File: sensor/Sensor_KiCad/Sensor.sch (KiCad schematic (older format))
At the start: 32 parts, among them J1 Conn_01x02_Female, J2 Conn_01x02_Female, J3 Conn_01x02_Female, J4 Conn_01x02_Female, J5 Conn_01x02_Female, J6 Conn_01x02_Female, J7 Conn_01x02_Female, J8 Conn_01x02_Female, U1 LM358, U2 LM358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

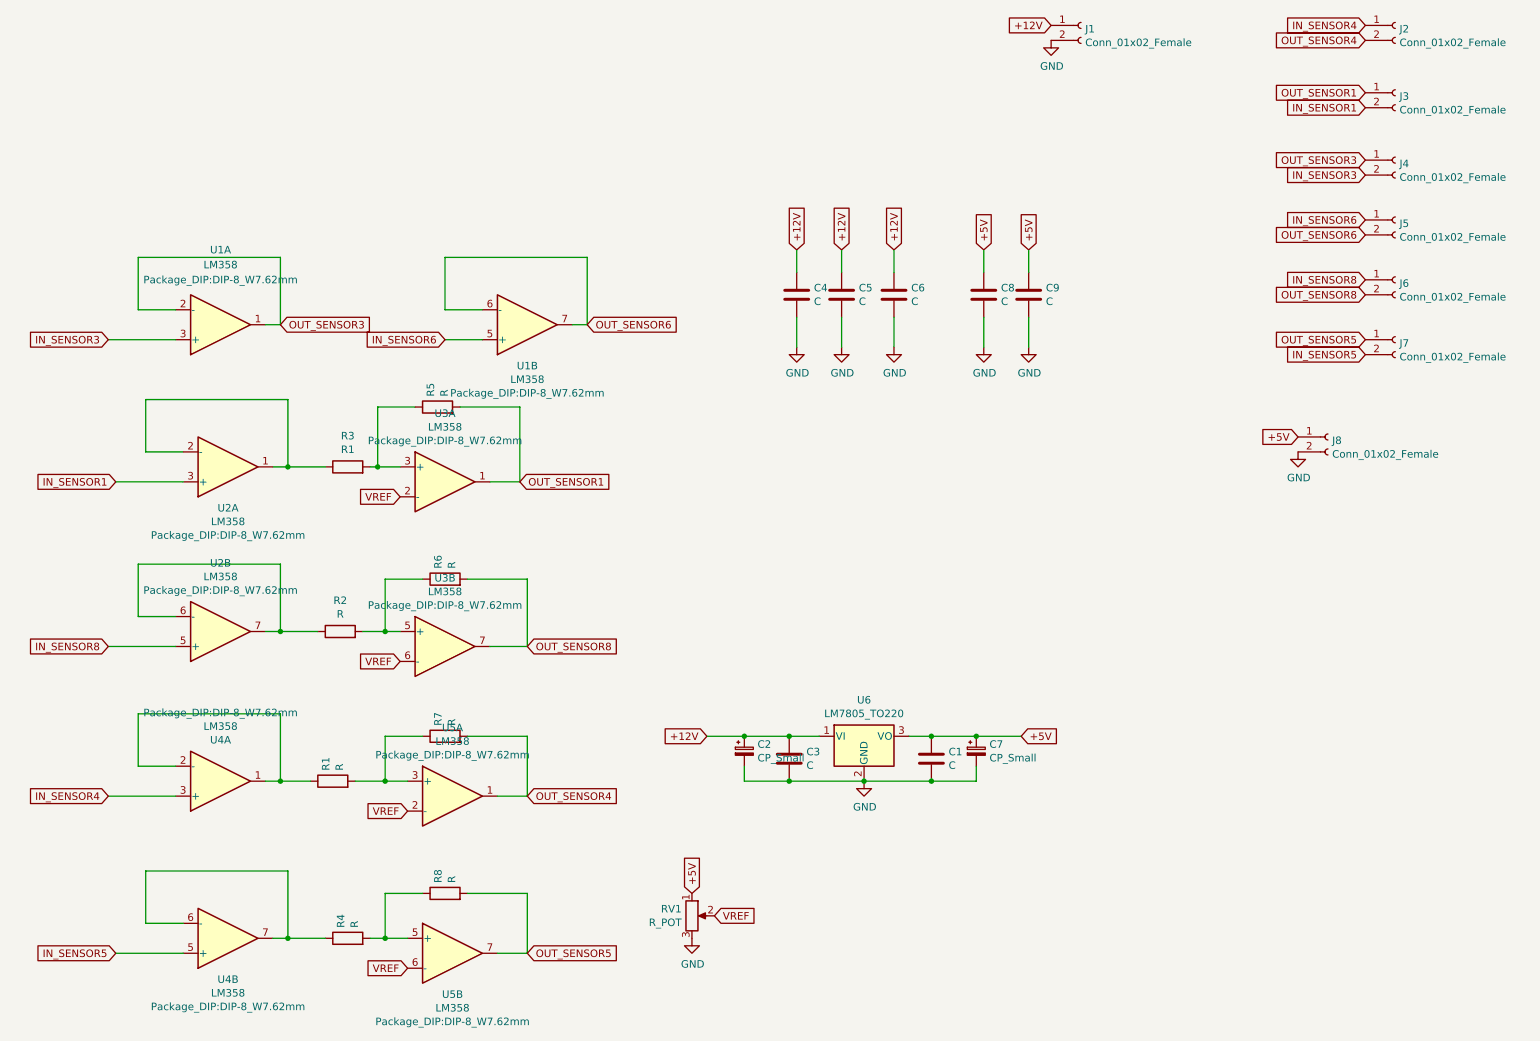
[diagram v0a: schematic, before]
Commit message: Kicad projects finished
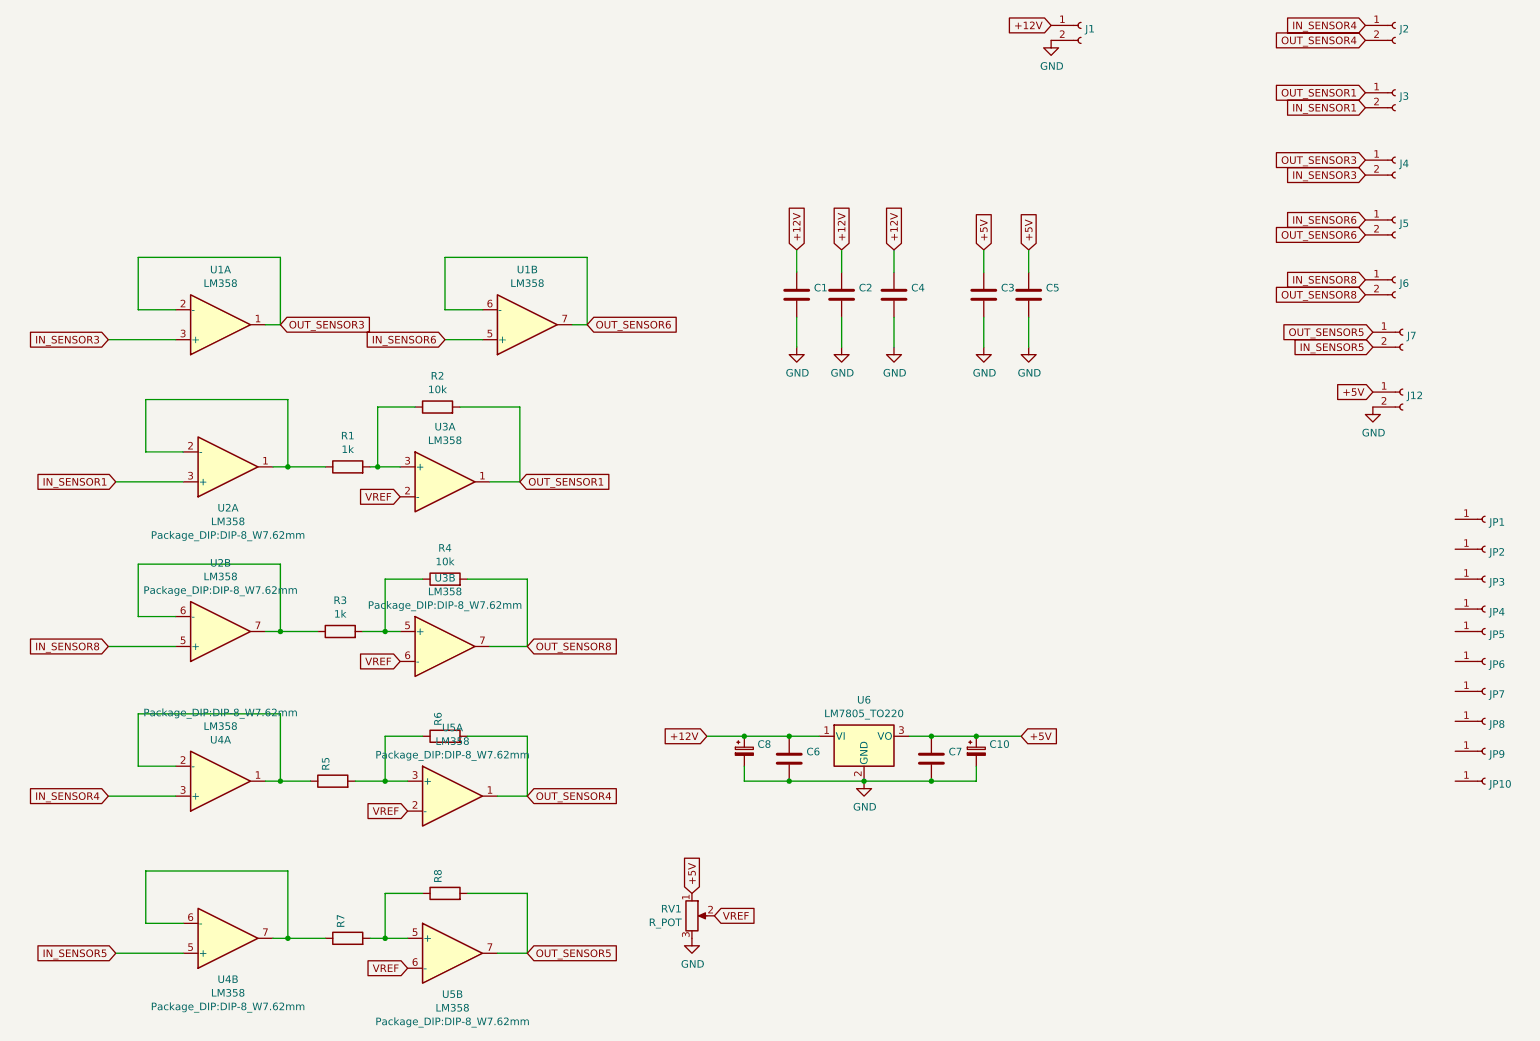
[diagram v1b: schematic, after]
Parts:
- added JP1, JP10, JP2, JP3, JP4, JP5, JP6, JP7, JP8, JP9: Conn_01x01_Female, Connector_Wire:SolderWire-0.5sqmm_1x01_D0.9mm_OD2.1mm, symbol Connector:Conn_01x01_Female
- C1: renamed from C4; footprint Capacitor_THT:C_Disc_D3.0mm_W1.6mm_P2.50mm -> Capacitor_THT:C_Disc_D4.3mm_W1.9mm_P5.00mm
- C2: renamed from C5; footprint Capacitor_THT:C_Disc_D3.0mm_W1.6mm_P2.50mm -> Capacitor_THT:C_Disc_D4.3mm_W1.9mm_P5.00mm
- C3: renamed from C8; footprint Capacitor_THT:C_Disc_D3.0mm_W1.6mm_P2.50mm -> Capacitor_THT:C_Disc_D4.3mm_W1.9mm_P5.00mm
- C4: renamed from C6; footprint Capacitor_THT:C_Disc_D3.0mm_W1.6mm_P2.50mm -> Capacitor_THT:C_Disc_D4.3mm_W1.9mm_P5.00mm
- C5: renamed from C9; footprint Capacitor_THT:C_Disc_D3.0mm_W1.6mm_P2.50mm -> Capacitor_THT:C_Disc_D4.3mm_W1.9mm_P5.00mm
- R1: renamed from R3; value R1 -> 1k; footprint Resistor_THT:R_Axial_DIN0207_L6.3mm_D2.5mm_P15.24mm_Horizontal -> Resistor_THT:R_Axial_DIN0204_L3.6mm_D1.6mm_P7.62mm_Horizontal
- R2: renamed from R5; value R -> 10k; footprint Resistor_THT:R_Axial_DIN0207_L6.3mm_D2.5mm_P15.24mm_Horizontal -> Resistor_THT:R_Axial_DIN0204_L3.6mm_D1.6mm_P7.62mm_Horizontal
- R3: renamed from R2; value R -> 1k; footprint Resistor_THT:R_Axial_DIN0207_L6.3mm_D2.5mm_P15.24mm_Horizontal -> Resistor_THT:R_Axial_DIN0204_L3.6mm_D1.6mm_P7.62mm_Horizontal
- R4: renamed from R6; value R -> 10k; footprint Resistor_THT:R_Axial_DIN0207_L6.3mm_D2.5mm_P15.24mm_Horizontal -> Resistor_THT:R_Axial_DIN0204_L3.6mm_D1.6mm_P7.62mm_Horizontal
- R5: renamed from R1; footprint Resistor_THT:R_Axial_DIN0207_L6.3mm_D2.5mm_P15.24mm_Horizontal -> Resistor_THT:R_Axial_DIN0204_L3.6mm_D1.6mm_P7.62mm_Horizontal
- R6: renamed from R7; footprint Resistor_THT:R_Axial_DIN0207_L6.3mm_D2.5mm_P15.24mm_Horizontal -> Resistor_THT:R_Axial_DIN0204_L3.6mm_D1.6mm_P7.62mm_Horizontal
- R7: renamed from R4; footprint Resistor_THT:R_Axial_DIN0207_L6.3mm_D2.5mm_P15.24mm_Horizontal -> Resistor_THT:R_Axial_DIN0204_L3.6mm_D1.6mm_P7.62mm_Horizontal
- R8: footprint Resistor_THT:R_Axial_DIN0207_L6.3mm_D2.5mm_P15.24mm_Horizontal -> Resistor_THT:R_Axial_DIN0204_L3.6mm_D1.6mm_P7.62mm_Horizontal
- renumbered C7 to C10, C3 to C6, C1 to C7, C2 to C8, J8 to J12
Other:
- moved on the sheet: J12, J7

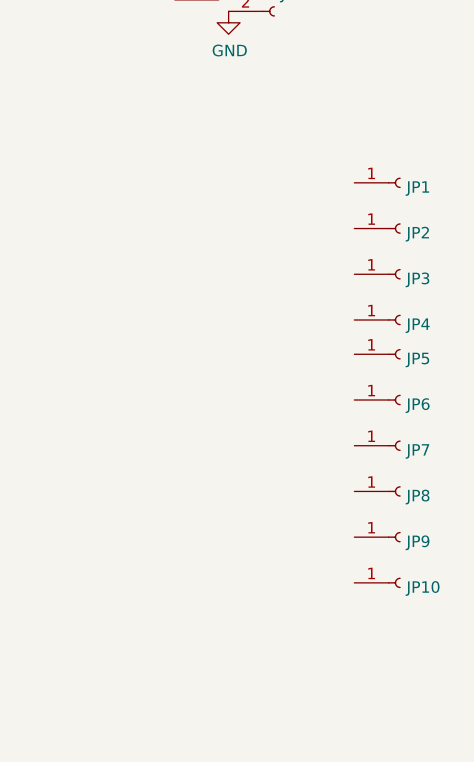
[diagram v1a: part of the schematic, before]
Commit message: corrected kiCad errors
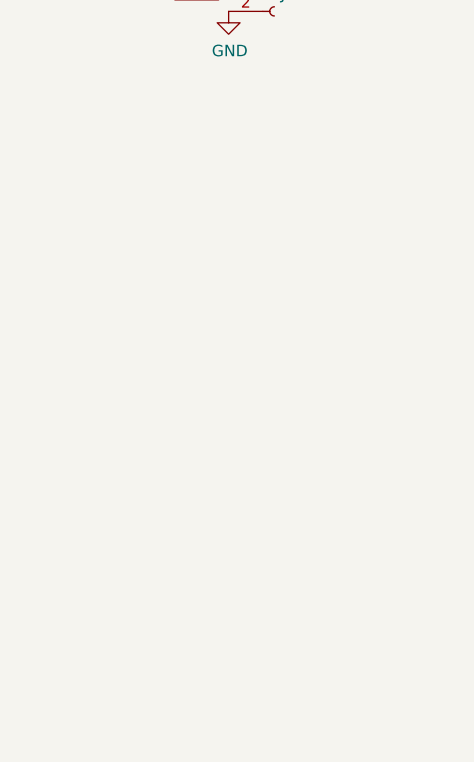
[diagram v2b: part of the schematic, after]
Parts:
- removed JP1, JP10, JP2, JP3, JP4, JP5, JP6, JP7, JP8, JP9: Conn_01x01_Female, Connector_Wire:SolderWire-0.5sqmm_1x01_D0.9mm_OD2.1mm, symbol Connector:Conn_01x01_Female
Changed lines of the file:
@@
-	1    0    0    -1
-$EndComp
-$Comp
-L Connector:Conn_01x01_Female JP1
-U 1 1 60164CE5
-P 10500 4150
-F 0 "JP1" H 10528 4130 50  0000 L CNN
-F 1 "Conn_01x01_Female" H 10528 4085 50  0001 L CNN
-F 2 "Connector_Wire:SolderWire-0.5sqmm_1x01_D0.9mm_OD2.1mm" H 10500 4150 50  0001 C CNN
-F 3 "~" H 10500 4150 50  0001 C CNN
-	1    10500 4150
-	1    0    0    -1
-$EndComp
-$Comp
-L Connector:Conn_01x01_Female JP2
-U 1 1 60166FBA
-P 10500 4350
-F 0 "JP2" H 10528 4330 50  0000 L CNN
-F 1 "Conn_01x01_Female" H 10528 4285 50  0001 L CNN
-F 2 "Connector_Wire:SolderWire-0.5sqmm_1x01_D0.9mm_OD2.1mm" H 10500 4350 50  0001 C CNN
-F 3 "~" H 10500 4350 50  0001 C CNN
-	1    10500 4350
-	1    0    0    -1
-$EndComp
-$Comp
-L Connector:Conn_01x01_Female JP3
-U 1 1 6016AD77
-P 10500 4550
-F 0 "JP3" H 10528 4530 50  0000 L CNN
-F 1 "Conn_01x01_Female" H 10528 4485 50  0001 L CNN
-F 2 "Connector_Wire:SolderWire-0.5sqmm_1x01_D0.9mm_OD2.1mm" H 10500 4550 50  0001 C CNN
-F 3 "~" H 10500 4550 50  0001 C CNN
-	1    10500 4550
-	1    0    0    -1
-$EndComp
-$Comp
-L Connector:Conn_01x01_Female JP4
-U 1 1 6016AD7D
-P 10500 4750
-F 0 "JP4" H 10528 4730 50  0000 L CNN
-F 1 "Conn_01x01_Female" H 10528 4685 50  0001 L CNN
-F 2 "Connector_Wire:SolderWire-0.5sqmm_1x01_D0.9mm_OD2.1mm" H 10500 4750 50  0001 C CNN
-F 3 "~" H 10500 4750 50  0001 C CNN
-	1    10500 4750
-	1    0    0    -1
-$EndComp
-$Comp
-L Connector:Conn_01x01_Female JP5
-U 1 1 6016EDA1
-P 10500 4900
-F 0 "JP5" H 10528 4880 50  0000 L CNN
-F 1 "Conn_01x01_Female" H 10528 4835 50  0001 L CNN
-F 2 "Connector_Wire:SolderWire-0.5sqmm_1x01_D0.9mm_OD2.1mm" H 10500 4900 50  0001 C CNN
-F 3 "~" H 10500 4900 50  0001 C CNN
-	1    10500 4900
-	1    0    0    -1
-$EndComp
-$Comp
-L Connector:Conn_01x01_Female JP6
-U 1 1 6016EDA7
-P 10500 5100
-F 0 "JP6" H 10528 5080 50  0000 L CNN
-F 1 "Conn_01x01_Female" H 10528 5035 50  0001 L CNN
-F 2 "Connector_Wire:SolderWire-0.5sqmm_1x01_D0.9mm_OD2.1mm" H 10500 5100 50  0001 C CNN
-F 3 "~" H 10500 5100 50  0001 C CNN
-	1    10500 5100
-	1    0    0    -1
-$EndComp
-$Comp
-L Connector:Conn_01x01_Female JP8
-U 1 1 6016EDB3
-P 10500 5500
-F 0 "JP8" H 10528 5480 50  0000 L CNN
-F 1 "Conn_01x01_Female" H 10528 5435 50  0001 L CNN
-F 2 "Connector_Wire:SolderWire-0.5sqmm_1x01_D0.9mm_OD2.1mm" H 10500 5500 50  0001 C CNN
-F 3 "~" H 10500 5500 50  0001 C CNN
-	1    10500 5500
-	1    0    0    -1
-$EndComp
-$Comp
-L Connector:Conn_01x01_Female JP7
-U 1 1 6016EDAD
-P 10500 5300
-F 0 "JP7" H 10528 5280 50  0000 L CNN
-F 1 "Conn_01x01_Female" H 10528 5235 50  0001 L CNN
-F 2 "Connector_Wire:SolderWire-0.5sqmm_1x01_D0.9mm_OD2.1mm" H 10500 5300 50  0001 C CNN
-F 3 "~" H 10500 5300 50  0001 C CNN
-	1    10500 5300
-	1    0    0    -1
-$EndComp
-$Comp
-L Connector:Conn_01x01_Female JP10
-U 1 1 60176F4E
-P 10500 5900
-F 0 "JP10" H 10528 5880 50  0000 L CNN
-F 1 "Conn_01x01_Female" H 10528 5835 50  0001 L CNN
-F 2 "Connector_Wire:SolderWire-0.5sqmm_1x01_D0.9mm_OD2.1mm" H 10500 5900 50  0001 C CNN
-F 3 "~" H 10500 5900 50  0001 C CNN
-	1    10500 5900
-	1    0    0    -1
-$EndComp
-$Comp
-L Connector:Conn_01x01_Female JP9
-U 1 1 60176F54
-P 10500 5700
-F 0 "JP9" H 10528 5680 50  0000 L CNN
-F 1 "Conn_01x01_Female" H 10528 5635 50  0001 L CNN
-F 2 "Connector_Wire:SolderWire-0.5sqmm_1x01_D0.9mm_OD2.1mm" H 10500 5700 50  0001 C CNN
-F 3 "~" H 10500 5700 50  0001 C CNN
-	1    10500 5700
 	1    0    0    -1
 $EndComp
